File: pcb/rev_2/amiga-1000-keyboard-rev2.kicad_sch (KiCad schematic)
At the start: 235 parts, among them J1 AMIGA, J2 USB-C, J3 ISP, SW1 ESC, SW10 F9, SW11 F10, SW12 HELP, SW13 `, SW14 1, SW15 2, SW16 3, SW17 4, SW18 5, SW19 6, SW2 F1, SW20 7, SW21 8, SW22 9, SW23 0, SW24 -, SW25 =, SW26 \\, SW27 UP, SW28 TAB, SW29 Q, SW3 F2, SW30 W, SW31 E, SW32 R, SW33 T, SW34 Y, SW35 U, SW36 I, SW37 O, SW38 P, SW39 [, SW4 F3, SW40 ], SW41 RETURN, SW42 LEFT, SW43 CAPS LOCK, SW44 A, SW45 S, SW46 D, SW47 F, SW48 G, SW49 H, SW5 F4, SW50 J, SW51 K, SW52 L, SW53 ;, SW54 ', SW55 (RET) INTL, SW56 DEL, SW57 RIGHT, SW58 L SHIFT INTL, SW59 Z, SW6 F5, SW60 X, SW61 C, SW62 V, SW63 B, SW64 N, SW65 M, SW66 ,, SW67 ., SW68 /, SW69 SPACE, SW7 F6, SW70 BACKSPACE, SW71 DOWN, SW72 KP 9, SW73 KP 6, SW74 KP 3, SW75 KP ., SW76 KP 8, SW77 KP 5, SW78 KP 2, SW79 KP ENTER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

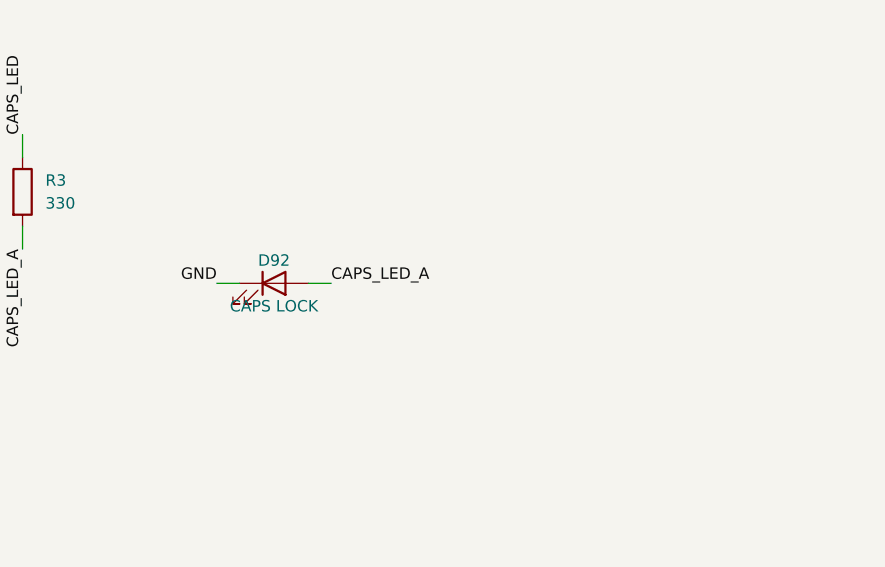
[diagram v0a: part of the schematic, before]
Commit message: take mitsumi or mx switches on rev 2, with a caps lock led for each.
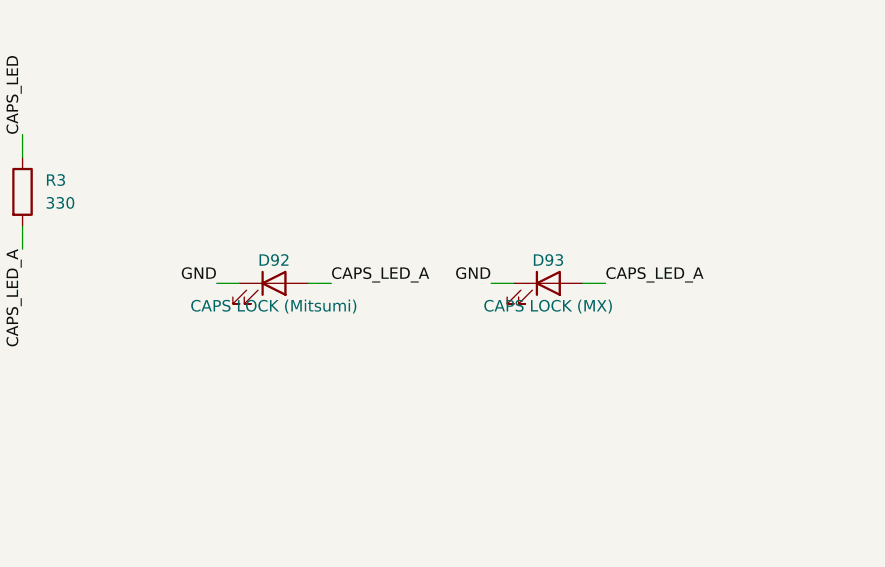
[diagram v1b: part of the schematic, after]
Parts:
- added D93: CAPS LOCK (MX), amiga1000:Hybrid_A1000_MX_LED, symbol Device:LED
- D92: value CAPS LOCK -> CAPS LOCK (Mitsumi); Part LED fitted in the Caps Lock switch, salvaged -> LED fitted in the Mitsumi Caps Lock switch, salvaged; now left out of the parts list
- SW1, SW12, SW14, SW15, SW16, SW17, SW18, SW19, SW20, SW21, SW22, SW23, SW24, SW25, SW26, SW27, SW29, SW30, SW31, SW32, SW33, SW34, SW35, SW36, SW37, SW38, SW39, SW40, SW42, SW43, SW44, SW45, SW46, SW47, SW48, SW49, SW50, SW51, SW52, SW53, SW54, SW55, SW56, SW57, SW58, SW59, SW60, SW61, SW62, SW63, SW64, SW65, SW66, SW67, SW68, SW71, SW72, SW73, SW74, SW75, SW76, SW77, SW78, SW80, SW81, SW82, SW84, SW88: footprint amiga1000:Mitsumi_A1000_Switch -> amiga1000:Hybrid_A1000_1U; Part Mitsumi standard mechanical Type 2 (KCT) keyswitch, salvaged -> Mitsumi KCT (salvaged) or Cherry MX keyswitch
- SW10, SW11, SW13, SW2, SW3, SW4, SW5, SW6, SW7, SW8, SW85, SW86, SW89, SW9, SW90: footprint amiga1000:Mitsumi_A1000_Switch -> amiga1000:Hybrid_A1000_1.25U; Part Mitsumi standard mechanical Type 2 (KCT) keyswitch, salvaged -> Mitsumi KCT (salvaged) or Cherry MX keyswitch
- SW28, SW70: footprint amiga1000:Mitsumi_A1000_Switch -> amiga1000:Hybrid_A1000_1.75U; Part Mitsumi standard mechanical Type 2 (KCT) keyswitch, salvaged -> Mitsumi KCT (salvaged) or Cherry MX keyswitch
- SW41: Part Mitsumi standard mechanical Type 2 (KCT) keyswitch, salvaged -> Mitsumi KCT (salvaged) or Cherry MX keyswitch
- SW69: footprint amiga1000:Mitsumi_A1000_Switch -> amiga1000:Hybrid_A1000_7.5U; Part Mitsumi standard mechanical Type 2 (KCT) keyswitch, salvaged -> Mitsumi KCT (salvaged) or Cherry MX keyswitch
- SW79, SW83, SW91: footprint amiga1000:Mitsumi_A1000_Switch -> amiga1000:Hybrid_A1000_2U; Part Mitsumi standard mechanical Type 2 (KCT) keyswitch, salvaged -> Mitsumi KCT (salvaged) or Cherry MX keyswitch
- SW87: footprint amiga1000:Mitsumi_A1000_Switch -> amiga1000:Hybrid_A1000_2.5U; Part Mitsumi standard mechanical Type 2 (KCT) keyswitch, salvaged -> Mitsumi KCT (salvaged) or Cherry MX keyswitch
- SW92: footprint amiga1000:Mitsumi_A1000_Switch -> amiga1000:Hybrid_A1000_1.5U; Part Mitsumi standard mechanical Type 2 (KCT) keyswitch, salvaged -> Mitsumi KCT (salvaged) or Cherry MX keyswitch
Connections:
- net CAPS_LED_A: now also D93.2 (A)
- net GND: now also D93.1 (K)

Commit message: give return a hybrid footprint with a vertical stabiliser, after henryk's us return.
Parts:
- SW41: footprint amiga1000:Mitsumi_A1000_Switch -> amiga1000:Hybrid_A1000_Return
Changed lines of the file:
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@@
 			)
 		)
-		(property "Footprint" "amiga1000:Mitsumi_A1000_Switch"
+		(property "Footprint" "amiga1000:Hybrid_A1000_Return"
 			(at 134.62 541.02 0)
 			(hide yes)

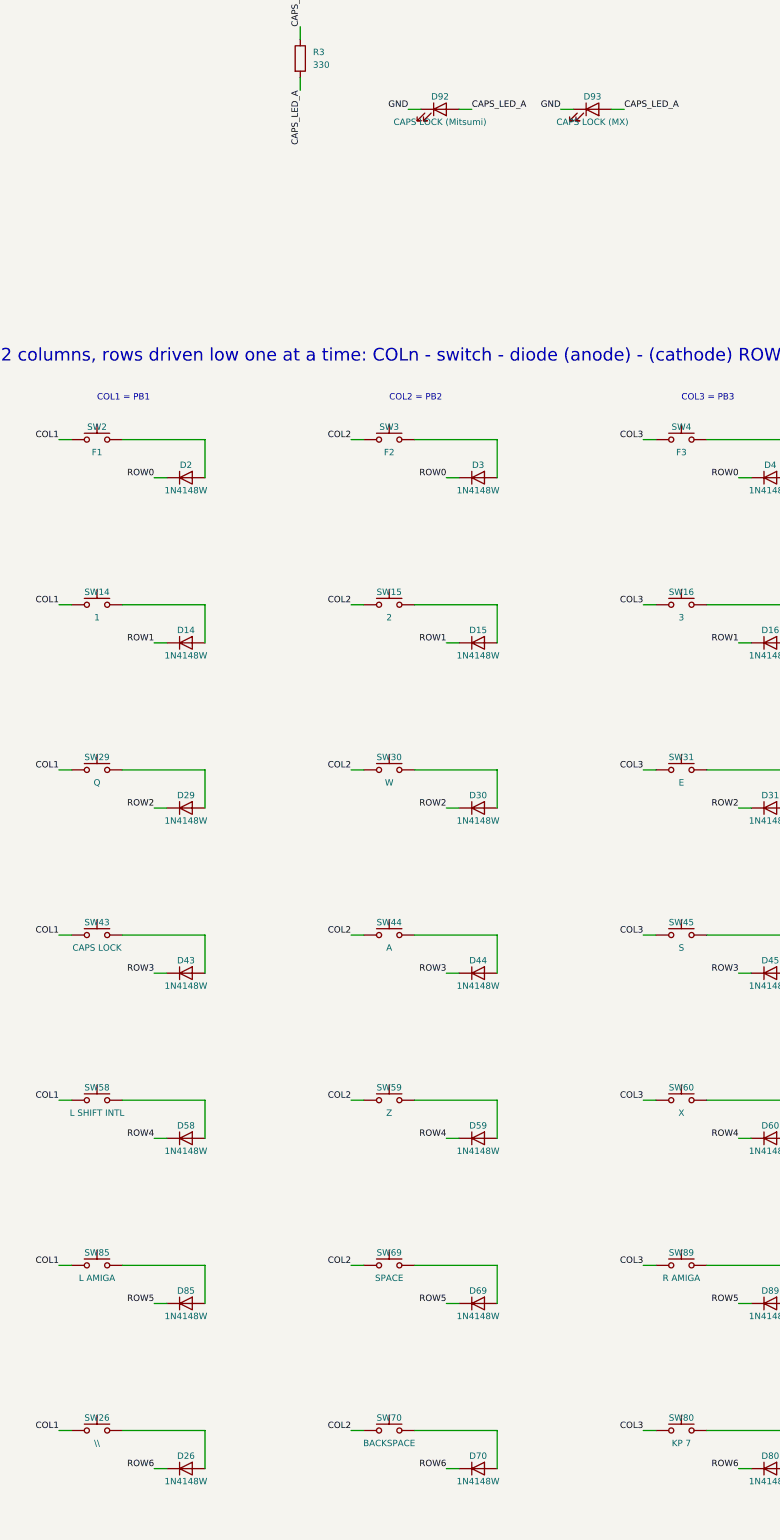
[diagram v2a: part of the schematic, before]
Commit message: take cherry mx switches only on rev 2; rev 1 stays the mitsumi board.
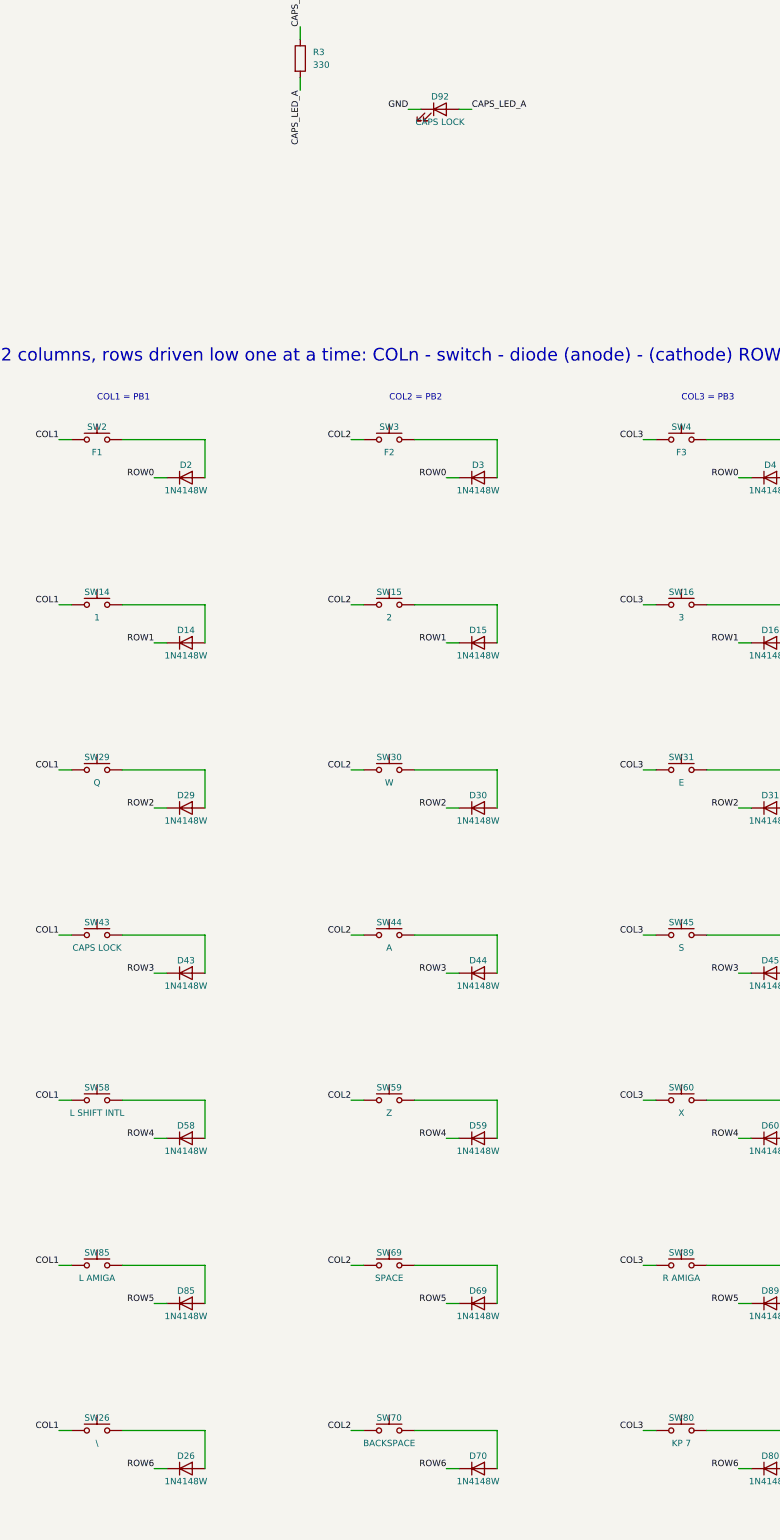
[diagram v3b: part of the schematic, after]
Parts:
- removed D93: CAPS LOCK (MX), amiga1000:Hybrid_A1000_MX_LED, symbol Device:LED
- D92: value CAPS LOCK (Mitsumi) -> CAPS LOCK; footprint amiga1000:Mitsumi_A1000_CapsLock_LED -> amiga1000:MX_A1000_LED; Part LED fitted in the Mitsumi Caps Lock switch, salvaged -> 3 mm LED through a Cherry MX switch
- SW1, SW12, SW14, SW15, SW16, SW17, SW18, SW19, SW20, SW21, SW22, SW23, SW24, SW25, SW27, SW29, SW30, SW31, SW32, SW33, SW34, SW35, SW36, SW37, SW38, SW39, SW40, SW42, SW43, SW44, SW45, SW46, SW47, SW48, SW49, SW50, SW51, SW52, SW53, SW54, SW55, SW56, SW57, SW58, SW59, SW60, SW61, SW62, SW63, SW64, SW65, SW66, SW67, SW68, SW71, SW72, SW73, SW74, SW75, SW76, SW77, SW78, SW80, SW81, SW82, SW84, SW88: footprint amiga1000:Hybrid_A1000_1U -> amiga1000:MX_A1000_1U; Part Mitsumi KCT (salvaged) or Cherry MX keyswitch -> Cherry MX (or compatible) keyswitch
- SW10, SW11, SW13, SW2, SW3, SW4, SW5, SW6, SW7, SW8, SW85, SW86, SW89, SW9, SW90: footprint amiga1000:Hybrid_A1000_1.25U -> amiga1000:MX_A1000_1.25U; Part Mitsumi KCT (salvaged) or Cherry MX keyswitch -> Cherry MX (or compatible) keyswitch
- SW26: value \\ -> \; footprint amiga1000:Hybrid_A1000_1U -> amiga1000:MX_A1000_1U; Part Mitsumi KCT (salvaged) or Cherry MX keyswitch -> Cherry MX (or compatible) keyswitch
- SW28, SW70: footprint amiga1000:Hybrid_A1000_1.75U -> amiga1000:MX_A1000_1.75U; Part Mitsumi KCT (salvaged) or Cherry MX keyswitch -> Cherry MX (or compatible) keyswitch
- SW41: footprint amiga1000:Hybrid_A1000_Return -> amiga1000:MX_A1000_Return; Part Mitsumi KCT (salvaged) or Cherry MX keyswitch -> Cherry MX (or compatible) keyswitch
- SW69: footprint amiga1000:Hybrid_A1000_7.5U -> amiga1000:MX_A1000_7.5U; Part Mitsumi KCT (salvaged) or Cherry MX keyswitch -> Cherry MX (or compatible) keyswitch
- SW79, SW83, SW91: footprint amiga1000:Hybrid_A1000_2U -> amiga1000:MX_A1000_2U; Part Mitsumi KCT (salvaged) or Cherry MX keyswitch -> Cherry MX (or compatible) keyswitch
- SW87: footprint amiga1000:Hybrid_A1000_2.5U -> amiga1000:MX_A1000_LShift; Part Mitsumi KCT (salvaged) or Cherry MX keyswitch -> Cherry MX (or compatible) keyswitch
- SW92: footprint amiga1000:Hybrid_A1000_1.5U -> amiga1000:MX_A1000_LShift_ISO; Part Mitsumi KCT (salvaged) or Cherry MX keyswitch -> Cherry MX (or compatible) keyswitch

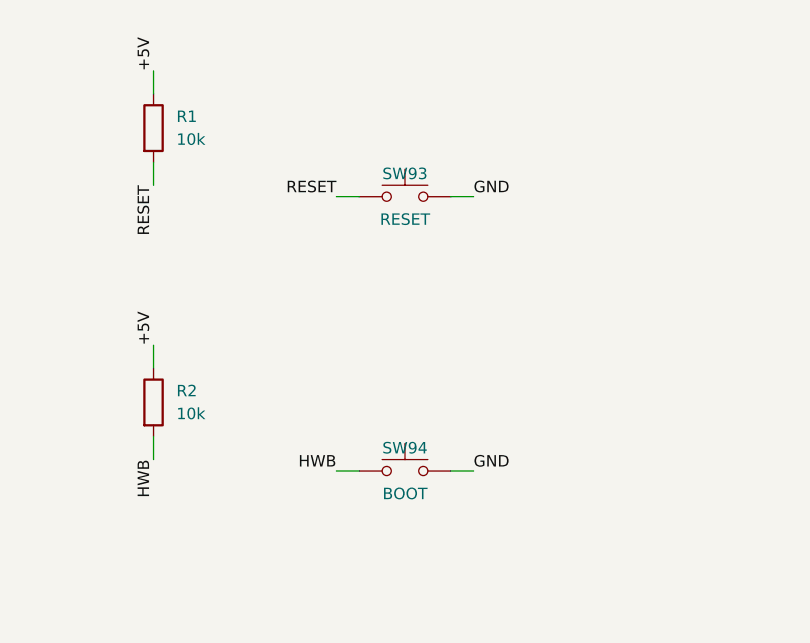
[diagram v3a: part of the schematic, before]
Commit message: move the rev 2 controller to the right and swap its buttons for jumper pads.
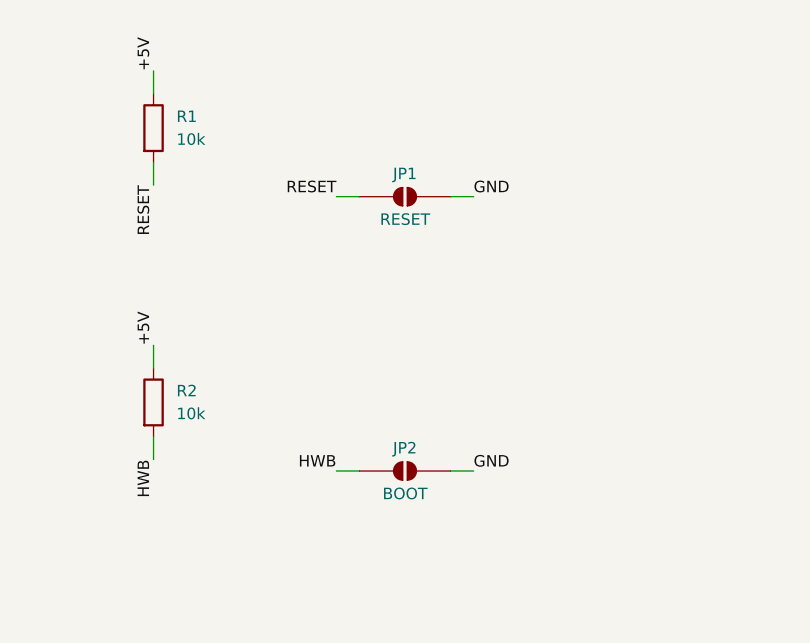
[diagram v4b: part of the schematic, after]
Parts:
- removed SW93: RESET, Button_Switch_SMD:SW_Push_1P1T_XKB_TS-1187A, symbol Switch:SW_Push
- removed SW94: BOOT, Button_Switch_SMD:SW_Push_1P1T_XKB_TS-1187A, symbol Switch:SW_Push
- added JP1: RESET, Jumper:SolderJumper-2_P1.3mm_Open_RoundedPad1.0x1.5mm, symbol Jumper:SolderJumper_2_Open
- added JP2: BOOT, Jumper:SolderJumper-2_P1.3mm_Open_RoundedPad1.0x1.5mm, symbol Jumper:SolderJumper_2_Open
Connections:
- net GND: now also JP1.2 (B), JP2.2 (B)
- net HWB: now also JP2.1 (A)
- net RESET: now also JP1.1 (A)
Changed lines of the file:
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@@
 	)
 	(symbol
-		(lib_id "Switch:SW_Push")
+		(lib_id "Jumper:SolderJumper_2_Open")
 		(at 203.2 134.62 0)
 		(unit 1)
 		(exclude_from_sim no)
-		(in_bom yes)
+		(in_bom no)
 		(on_board yes)
 		(dnp no)
-		(property "Reference" "SW93"
+		(property "Reference" "JP1"
 			(at 203.2 132.08 0)
 			(effects
@@
 			)
 		)
-		(property "Footprint" "Button_Switch_SMD:SW_Push_1P1T_XKB_TS-1187A"
+		(property "Footprint" "Jumper:SolderJumper-2_P1.3mm_Open_RoundedPad1.0x1.5mm"
 			(at 203.2 134.62 0)
 			(hide yes)
@@
 			)
 		)
-		(property "Description" ""
-			(at 203.2 134.62 0)
-			(hide yes)
-			(effects
-				(font
-					(size 1.27 1.27)
-				)
-			)
-		)
-		(property "Part" "XKB TS-1187A tactile switch"
+		(property "Description" "Short to reset the 32U4"
+			(at 203.2 134.62 0)
+			(hide yes)
+			(effects
+				(font
+					(size 1.27 1.27)
+				)
+			)
+		)
+		(property "Part" "pads, shorted with tweezers"
 			(at 203.2 134.62 0)
 			(hide yes)
@@
 			(project "amiga-1000-keyboard-rev2"
 				(path "/8c4c0c0e-c260-5684-b55c-362c20f153e7"
-					(reference "SW93")
+					(reference "JP1")
 					(unit 1)
 				)
@@
 	)
 	(symbol
-		(lib_id "Switch:SW_Push")
+		(lib_id "Jumper:SolderJumper_2_Open")
 		(at 203.2 165.1 0)
 		(unit 1)
 		(exclude_from_sim no)
-		(in_bom yes)
+		(in_bom no)
 		(on_board yes)
 		(dnp no)
-		(property "Reference" "SW94"
+		(property "Reference" "JP2"
 			(at 203.2 162.56 0)
 			(effects
@@
 			)
 		)
-		(property "Footprint" "Button_Switch_SMD:SW_Push_1P1T_XKB_TS-1187A"
+		(property "Footprint" "Jumper:SolderJumper-2_P1.3mm_Open_RoundedPad1.0x1.5mm"
 			(at 203.2 165.1 0)
 			(hide yes)
@@
 			)
 		)
-		(property "Description" "Hold while pressing RESET to enter the USB (DFU) bootloader"
-			(at 203.2 165.1 0)
-			(hide yes)
-			(effects
-				(font
-					(size 1.27 1.27)
-				)
-			)
-		)
-		(property "Part" "XKB TS-1187A tactile switch"
+		(property "Description" "Short while shorting RESET to enter the USB (DFU) bootloader; firmware can also jump there"
+			(at 203.2 165.1 0)
+			(hide yes)
+			(effects
+				(font
+					(size 1.27 1.27)
+				)
+			)
+		)
+		(property "Part" "pads, shorted with tweezers"
 			(at 203.2 165.1 0)
 			(hide yes)
@@
 			(project "amiga-1000-keyboard-rev2"
 				(path "/8c4c0c0e-c260-5684-b55c-362c20f153e7"
-					(reference "SW94")
+					(reference "JP2")
 					(unit 1)
 				)

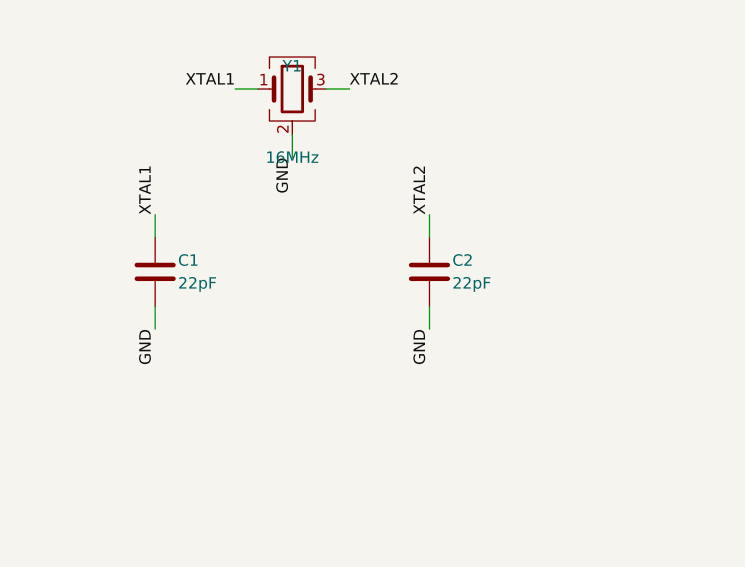
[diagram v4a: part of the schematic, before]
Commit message: add lcsc part numbers to rev 2, with 12 pf load caps for its 9 pf crystal.
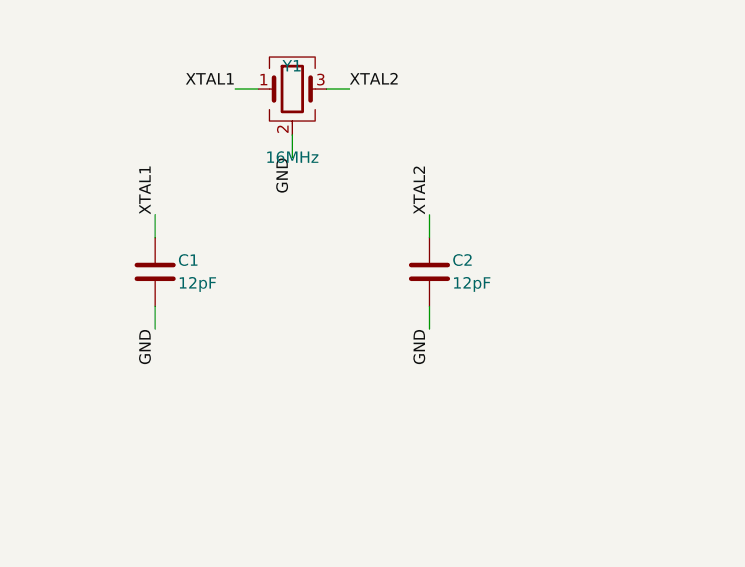
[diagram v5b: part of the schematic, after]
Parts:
- C1, C2: value 22pF -> 12pF; LCSC (none) -> C1547; Part 22 pF C0G 0402 -> 12 pF C0G 0402
- C10, C11, C8: LCSC (none) -> C52923
- C12, C7: LCSC (none) -> C19702
- C13, C14, C15: LCSC (none) -> C1523
- C3, C4, C5, C6, C9: LCSC (none) -> C1525
- D1, D10, D11, D12, D13, D14, D15, D16, D17, D18, D19, D2, D20, D21, D22, D23, D24, D25, D26, D27, D28, D29, D3, D30, D31, D32, D33, D34, D35, D36, D37, D38, D39, D4, D40, D41, D42, D43, D44, D45, D46, D47, D48, D49, D5, D50, D51, D52, D53, D54, D55, D56, D57, D58, D59, D6, D60, D61, D62, D63, D64, D65, D66, D67, D68, D69, D7, D70, D71, D72, D73, D74, D75, D76, D77, D78, D79, D8, D80, D81, D82, D83, D84, D85, D86, D87, D88, D89, D9, D90, D91: LCSC (none) -> C81598
- F1: LCSC (none) -> C70077
- FB1, FB2, FB3: LCSC (none) -> C1002
- J1: LCSC (none) -> C265102
- J2: LCSC (none) -> C165948
- R1, R2, R5, R6: LCSC (none) -> C25744
- R10, R9: LCSC (none) -> C25092
- R3: LCSC (none) -> C25104
- R4: LCSC (none) -> C25779
- R7, R8: LCSC (none) -> C25905
- U1: LCSC (none) -> C44854
- U2: LCSC (none) -> C3235557
- U3: LCSC (none) -> C7519
- Y1: LCSC (none) -> C13738; Part 16 MHz crystal, 3225, CL 20 pF -> 16 MHz crystal, 3225, CL 9 pF
